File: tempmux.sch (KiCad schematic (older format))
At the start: 15 parts, among them J2 Conn_02x07_Counter_Clockwise, U12 CD74HC4067SM

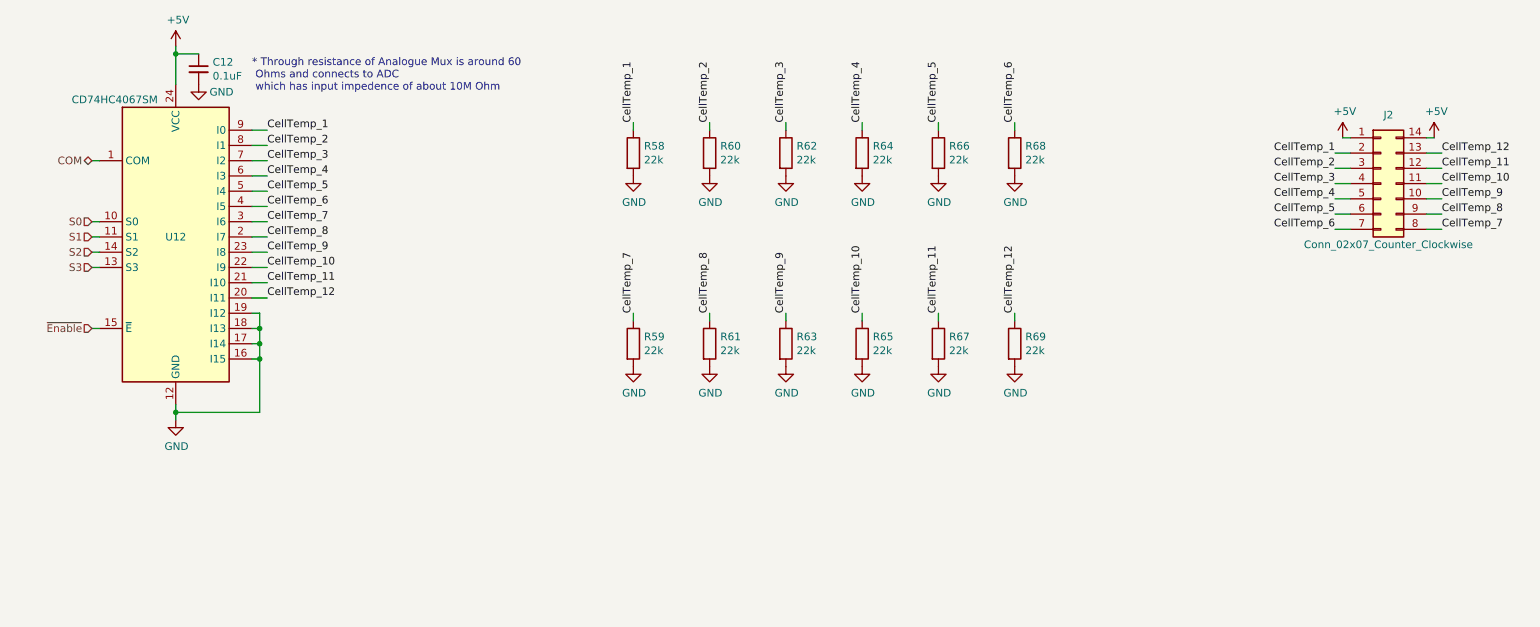
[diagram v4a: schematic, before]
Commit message: Added buttons + redid numbering
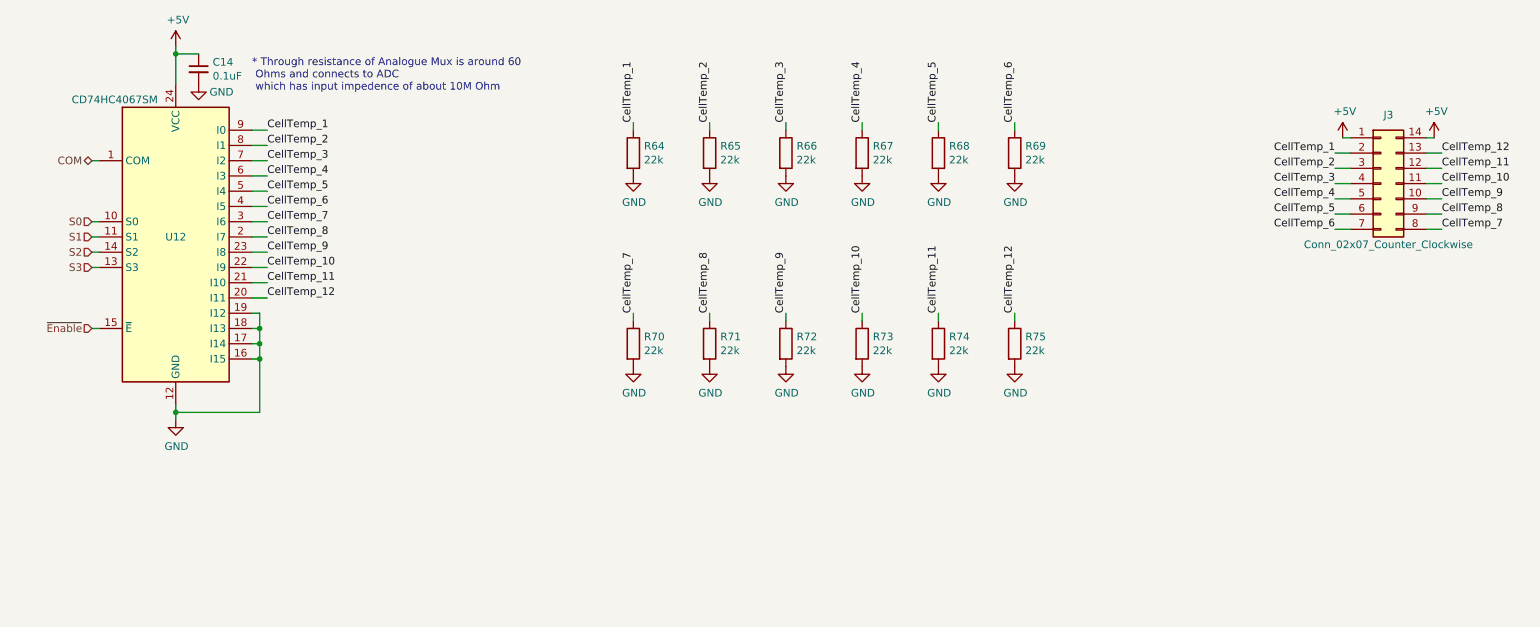
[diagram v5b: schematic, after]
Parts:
- renumbered C12 to C14, J2 to J3, R58 to R64, R60 to R65, R62 to R66, R64 to R67, R66 to R68, R68 to R69, R59 to R70, R61 to R71, R63 to R72, R65 to R73, R67 to R74, R69 to R75
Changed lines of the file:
@@
 P 2000 3400
 AR Path="/5F70A721/5F6868D9" Ref="#PWR?"  Part="1"
-AR Path="/5F70B1A3/5F6868D9" Ref="#PWR0153"  Part="1"
-F 0 "#PWR0153" H 2000 3150 50  0001 C CNN
+AR Path="/5F70B1A3/5F6868D9" Ref="#PWR078"  Part="1"
+F 0 "#PWR078" H 2000 3150 50  0001 C CNN
 F 1 "GND" H 2005 3227 50  0000 C CNN
 F 2 "" H 2000 3400 50  0001 C CNN
@@
 P 2150 1100
 AR Path="/5F70A721/5F6868E0" Ref="C?"  Part="1"
-AR Path="/5F70B1A3/5F6868E0" Ref="C12"  Part="1"
-F 0 "C12" H 2242 1146 50  0000 L CNN
+AR Path="/5F70B1A3/5F6868E0" Ref="C14"  Part="1"
+F 0 "C14" H 2242 1146 50  0000 L CNN
 F 1 "0.1uF" H 2242 1055 50  0000 L CNN
 F 2 "" H 2150 1100 50  0001 C CNN
@@
 P 2150 1200
 AR Path="/5F70A721/5F6868E6" Ref="#PWR?"  Part="1"
-AR Path="/5F70B1A3/5F6868E6" Ref="#PWR0154"  Part="1"
-F 0 "#PWR0154" H 2150 950 50  0001 C CNN
+AR Path="/5F70B1A3/5F6868E6" Ref="#PWR063"  Part="1"
+F 0 "#PWR063" H 2150 950 50  0001 C CNN
 F 1 "GND" H 2300 1150 50  0000 C CNN
 F 2 "" H 2150 1200 50  0001 C CNN
@@
 P 2000 950
 AR Path="/5F70A721/5F6868EC" Ref="#PWR?"  Part="1"
-AR Path="/5F70B1A3/5F6868EC" Ref="#PWR0155"  Part="1"
-F 0 "#PWR0155" H 2000 800 50  0001 C CNN
+AR Path="/5F70B1A3/5F6868EC" Ref="#PWR062"  Part="1"
+F 0 "#PWR062" H 2000 800 50  0001 C CNN
 F 1 "+5V" H 2015 1123 50  0000 C CNN
 F 2 "" H 2000 950 50  0001 C CNN
@@
 P 9900 1850
 AR Path="/5F70A721/5F68B135" Ref="J?"  Part="1"
-AR Path="/5F70B1A3/5F68B135" Ref="J2"  Part="1"
-F 0 "J2" H 9950 2300 50  0000 C CNN
+AR Path="/5F70B1A3/5F68B135" Ref="J3"  Part="1"
+F 0 "J3" H 9950 2300 50  0000 C CNN
 F 1 "Conn_02x07_Counter_Clockwise" H 9950 1450 50  0000 C CNN
 F 2 "" H 9900 1850 50  0001 C CNN
@@
 P 9650 1550
 AR Path="/5F70A721/5F68DF75" Ref="#PWR?"  Part="1"
-AR Path="/5F70B1A3/5F68DF75" Ref="#PWR0156"  Part="1"
-F 0 "#PWR0156" H 9650 1400 50  0001 C CNN
+AR Path="/5F70B1A3/5F68DF75" Ref="#PWR064"  Part="1"
+F 0 "#PWR064" H 9650 1400 50  0001 C CNN
 F 1 "+5V" H 9665 1723 50  0000 C CNN
 F 2 "" H 9650 1550 50  0001 C CNN
@@
 P 10250 1550
 AR Path="/5F70A721/5F68E7C7" Ref="#PWR?"  Part="1"
-AR Path="/5F70B1A3/5F68E7C7" Ref="#PWR0157"  Part="1"
-F 0 "#PWR0157" H 10250 1400 50  0001 C CNN
+AR Path="/5F70B1A3/5F68E7C7" Ref="#PWR065"  Part="1"
+F 0 "#PWR065" H 10250 1400 50  0001 C CNN
 F 1 "+5V" H 10265 1723 50  0000 C CNN
 F 2 "" H 10250 1550 50  0001 C CNN
@@
 	10200 1650 10300 1650
 $Comp
-L Device:R R58
+L Device:R R64
 U 1 1 5F69A862
 P 5000 1650
-F 0 "R58" H 5070 1696 50  0000 L CNN
+F 0 "R64" H 5070 1696 50  0000 L CNN
 F 1 "22k" H 5070 1605 50  0000 L CNN
 F 2 "" V 4930 1650 50  0001 C CNN
@@
 $EndComp
 $Comp
-L Device:R R60
+L Device:R R65
 U 1 1 5F69AE56
 P 5500 1650
-F 0 "R60" H 5570 1696 50  0000 L CNN
+F 0 "R65" H 5570 1696 50  0000 L CNN
 F 1 "22k" H 5570 1605 50  0000 L CNN
 F 2 "" V 5430 1650 50  0001 C CNN
@@
 $EndComp
 $Comp
-L Device:R R62
+L Device:R R66
 U 1 1 5F69AFF2
 P 6000 1650
-F 0 "R62" H 6070 1696 50  0000 L CNN
+F 0 "R66" H 6070 1696 50  0000 L CNN
 F 1 "22k" H 6070 1605 50  0000 L CNN
 F 2 "" V 5930 1650 50  0001 C CNN
@@
 $EndComp
 $Comp
-L Device:R R64
+L Device:R R67
 U 1 1 5F69B1F7
 P 6500 1650
-F 0 "R64" H 6570 1696 50  0000 L CNN
+F 0 "R67" H 6570 1696 50  0000 L CNN
 F 1 "22k" H 6570 1605 50  0000 L CNN
 F 2 "" V 6430 1650 50  0001 C CNN
@@
 $EndComp
 $Comp
-L Device:R R66
+L Device:R R68
 U 1 1 5F69B4CD
 P 7000 1650
-F 0 "R66" H 7070 1696 50  0000 L CNN
+F 0 "R68" H 7070 1696 50  0000 L CNN
 F 1 "22k" H 7070 1605 50  0000 L CNN
 F 2 "" V 6930 1650 50  0001 C CNN
@@
 $EndComp
 $Comp
-L Device:R R68
+L Device:R R69
 U 1 1 5F69B7DC
 P 7500 1650
-F 0 "R68" H 7570 1696 50  0000 L CNN
+F 0 "R69" H 7570 1696 50  0000 L CNN
 F 1 "22k" H 7570 1605 50  0000 L CNN
 F 2 "" V 7430 1650 50  0001 C CNN
@@
 $EndComp
 $Comp
-L Device:R R59
+L Device:R R70
 U 1 1 5F6A3EEE
 P 5000 2900
-F 0 "R59" H 5070 2946 50  0000 L CNN
+F 0 "R70" H 5070 2946 50  0000 L CNN
 F 1 "22k" H 5070 2855 50  0000 L CNN
 F 2 "" V 4930 2900 50  0001 C CNN
@@
 $EndComp
 $Comp
-L Device:R R61
+L Device:R R71
 U 1 1 5F6A3EF4
 P 5500 2900
-F 0 "R61" H 5570 2946 50  0000 L CNN
+F 0 "R71" H 5570 2946 50  0000 L CNN
 F 1 "22k" H 5570 2855 50  0000 L CNN
 F 2 "" V 5430 2900 50  0001 C CNN
@@
 $EndComp
 $Comp
-L Device:R R63
+L Device:R R72
 U 1 1 5F6A3EFA
 P 6000 2900
-F 0 "R63" H 6070 2946 50  0000 L CNN
+F 0 "R72" H 6070 2946 50  0000 L CNN
 F 1 "22k" H 6070 2855 50  0000 L CNN
 F 2 "" V 5930 2900 50  0001 C CNN
@@
 $EndComp
 $Comp
-L Device:R R65
+L Device:R R73
 U 1 1 5F6A3F00
 P 6500 2900
-F 0 "R65" H 6570 2946 50  0000 L CNN
+F 0 "R73" H 6570 2946 50  0000 L CNN
 F 1 "22k" H 6570 2855 50  0000 L CNN
 F 2 "" V 6430 2900 50  0001 C CNN
@@
 $EndComp
 $Comp
-L Device:R R67
+L Device:R R74
 U 1 1 5F6A3F06
 P 7000 2900
-F 0 "R67" H 7070 2946 50  0000 L CNN
+F 0 "R74" H 7070 2946 50  0000 L CNN
 F 1 "22k" H 7070 2855 50  0000 L CNN
 F 2 "" V 6930 2900 50  0001 C CNN
@@
 $EndComp
 $Comp
-L Device:R R69
+L Device:R R75
 U 1 1 5F6A3F0C
 P 7500 2900
-F 0 "R69" H 7570 2946 50  0000 L CNN
+F 0 "R75" H 7570 2946 50  0000 L CNN
 F 1 "22k" H 7570 2855 50  0000 L CNN
 F 2 "" V 7430 2900 50  0001 C CNN
@@
 P 5000 1800
 AR Path="/5F70A721/5F6A4A53" Ref="#PWR?"  Part="1"
-AR Path="/5F70B1A3/5F6A4A53" Ref="#PWR0158"  Part="1"
-F 0 "#PWR0158" H 5000 1550 50  0001 C CNN
+AR Path="/5F70B1A3/5F6A4A53" Ref="#PWR066"  Part="1"
+F 0 "#PWR066" H 5000 1550 50  0001 C CNN
 F 1 "GND" H 5005 1627 50  0000 C CNN
 F 2 "" H 5000 1800 50  0001 C CNN
@@
 P 5500 1800
 AR Path="/5F70A721/5F6A4F23" Ref="#PWR?"  Part="1"
-AR Path="/5F70B1A3/5F6A4F23" Ref="#PWR0159"  Part="1"
-F 0 "#PWR0159" H 5500 1550 50  0001 C CNN
+AR Path="/5F70B1A3/5F6A4F23" Ref="#PWR067"  Part="1"
+F 0 "#PWR067" H 5500 1550 50  0001 C CNN
 F 1 "GND" H 5505 1627 50  0000 C CNN
 F 2 "" H 5500 1800 50  0001 C CNN
@@
 P 6000 1800
 AR Path="/5F70A721/5F6A5197" Ref="#PWR?"  Part="1"
-AR Path="/5F70B1A3/5F6A5197" Ref="#PWR0160"  Part="1"
-F 0 "#PWR0160" H 6000 1550 50  0001 C CNN
+AR Path="/5F70B1A3/5F6A5197" Ref="#PWR068"  Part="1"
+F 0 "#PWR068" H 6000 1550 50  0001 C CNN
 F 1 "GND" H 6005 1627 50  0000 C CNN
 F 2 "" H 6000 1800 50  0001 C CNN
@@
 P 6500 1800
 AR Path="/5F70A721/5F6A5348" Ref="#PWR?"  Part="1"
-AR Path="/5F70B1A3/5F6A5348" Ref="#PWR0161"  Part="1"
-F 0 "#PWR0161" H 6500 1550 50  0001 C CNN
+AR Path="/5F70B1A3/5F6A5348" Ref="#PWR069"  Part="1"
+F 0 "#PWR069" H 6500 1550 50  0001 C CNN
 F 1 "GND" H 6505 1627 50  0000 C CNN
 F 2 "" H 6500 1800 50  0001 C CNN
@@
 P 7000 1800
 AR Path="/5F70A721/5F6A55E5" Ref="#PWR?"  Part="1"
-AR Path="/5F70B1A3/5F6A55E5" Ref="#PWR0162"  Part="1"
-F 0 "#PWR0162" H 7000 1550 50  0001 C CNN
+AR Path="/5F70B1A3/5F6A55E5" Ref="#PWR070"  Part="1"
+F 0 "#PWR070" H 7000 1550 50  0001 C CNN
 F 1 "GND" H 7005 1627 50  0000 C CNN
 F 2 "" H 7000 1800 50  0001 C CNN
@@
 P 7500 1800
 AR Path="/5F70A721/5F6A585F" Ref="#PWR?"  Part="1"
-AR Path="/5F70B1A3/5F6A585F" Ref="#PWR0163"  Part="1"
-F 0 "#PWR0163" H 7500 1550 50  0001 C CNN
+AR Path="/5F70B1A3/5F6A585F" Ref="#PWR071"  Part="1"
+F 0 "#PWR071" H 7500 1550 50  0001 C CNN
 F 1 "GND" H 7505 1627 50  0000 C CNN
 F 2 "" H 7500 1800 50  0001 C CNN
@@
 P 5000 3050
 AR Path="/5F70A721/5F6A59FF" Ref="#PWR?"  Part="1"
-AR Path="/5F70B1A3/5F6A59FF" Ref="#PWR0164"  Part="1"
-F 0 "#PWR0164" H 5000 2800 50  0001 C CNN
+AR Path="/5F70B1A3/5F6A59FF" Ref="#PWR072"  Part="1"
+F 0 "#PWR072" H 5000 2800 50  0001 C CNN
 F 1 "GND" H 5005 2877 50  0000 C CNN
 F 2 "" H 5000 3050 50  0001 C CNN
@@
 P 5500 3050
 AR Path="/5F70A721/5F6A5CE6" Ref="#PWR?"  Part="1"
-AR Path="/5F70B1A3/5F6A5CE6" Ref="#PWR0165"  Part="1"
-F 0 "#PWR0165" H 5500 2800 50  0001 C CNN
+AR Path="/5F70B1A3/5F6A5CE6" Ref="#PWR073"  Part="1"
+F 0 "#PWR073" H 5500 2800 50  0001 C CNN
 F 1 "GND" H 5505 2877 50  0000 C CNN
 F 2 "" H 5500 3050 50  0001 C CNN
@@
 P 6000 3050
 AR Path="/5F70A721/5F6A5EEC" Ref="#PWR?"  Part="1"
-AR Path="/5F70B1A3/5F6A5EEC" Ref="#PWR0166"  Part="1"
-F 0 "#PWR0166" H 6000 2800 50  0001 C CNN
+AR Path="/5F70B1A3/5F6A5EEC" Ref="#PWR074"  Part="1"
+F 0 "#PWR074" H 6000 2800 50  0001 C CNN
 F 1 "GND" H 6005 2877 50  0000 C CNN
 F 2 "" H 6000 3050 50  0001 C CNN
@@
 P 6500 3050
 AR Path="/5F70A721/5F6A6093" Ref="#PWR?"  Part="1"
-AR Path="/5F70B1A3/5F6A6093" Ref="#PWR0167"  Part="1"
-F 0 "#PWR0167" H 6500 2800 50  0001 C CNN
+AR Path="/5F70B1A3/5F6A6093" Ref="#PWR075"  Part="1"
+F 0 "#PWR075" H 6500 2800 50  0001 C CNN
 F 1 "GND" H 6505 2877 50  0000 C CNN
 F 2 "" H 6500 3050 50  0001 C CNN
@@
 P 7000 3050
 AR Path="/5F70A721/5F6A622C" Ref="#PWR?"  Part="1"
-AR Path="/5F70B1A3/5F6A622C" Ref="#PWR0168"  Part="1"
-F 0 "#PWR0168" H 7000 2800 50  0001 C CNN
+AR Path="/5F70B1A3/5F6A622C" Ref="#PWR076"  Part="1"
+F 0 "#PWR076" H 7000 2800 50  0001 C CNN
 F 1 "GND" H 7005 2877 50  0000 C CNN
 F 2 "" H 7000 3050 50  0001 C CNN
@@
 P 7500 3050
 AR Path="/5F70A721/5F6A6421" Ref="#PWR?"  Part="1"
-AR Path="/5F70B1A3/5F6A6421" Ref="#PWR0169"  Part="1"
-F 0 "#PWR0169" H 7500 2800 50  0001 C CNN
+AR Path="/5F70B1A3/5F6A6421" Ref="#PWR077"  Part="1"
+F 0 "#PWR077" H 7500 2800 50  0001 C CNN
 F 1 "GND" H 7505 2877 50  0000 C CNN
 F 2 "" H 7500 3050 50  0001 C CNN

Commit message: Added PCB temp sensors and redit numberings
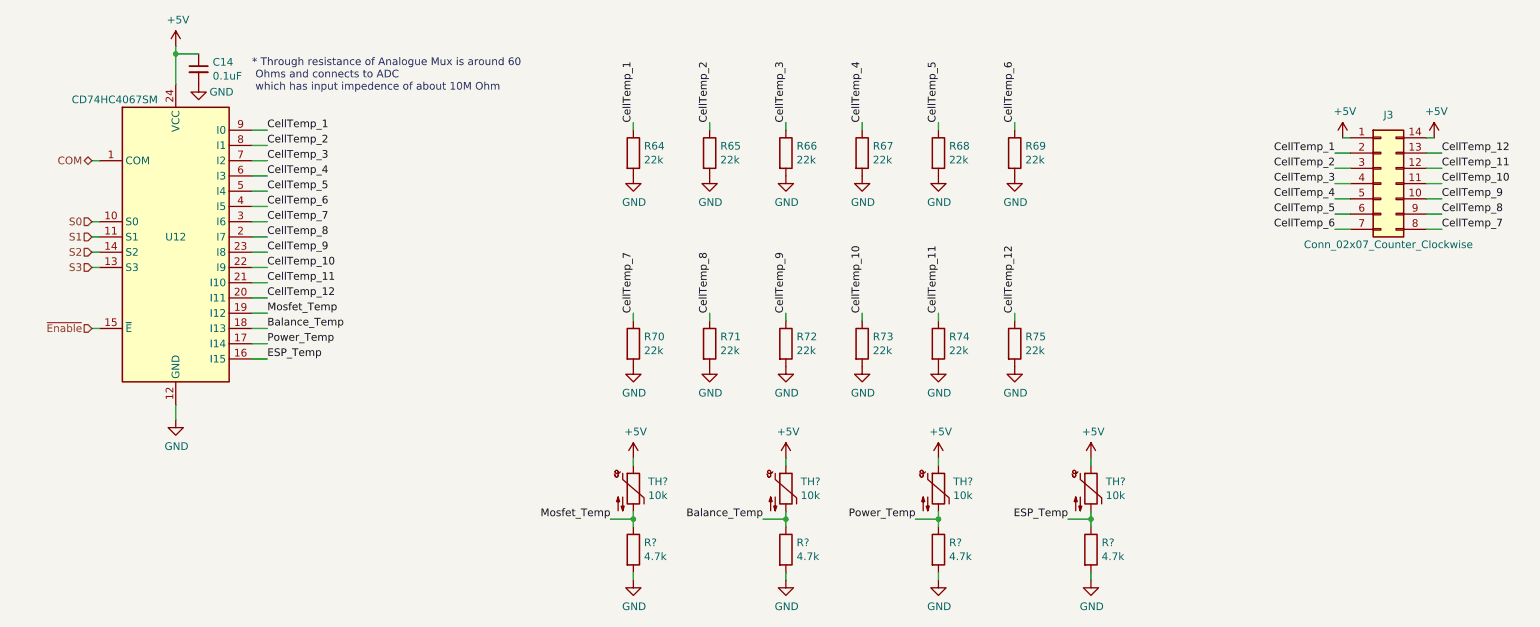
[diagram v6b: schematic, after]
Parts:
- added R? (x4): 4.7k, symbol Device:R
- added TH? (x4): 10k, symbol Device:Thermistor_NTC
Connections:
- net +5V: now also TH?.1, TH?.1, TH?.1, TH?.1
- net GND: now also R?.2, R?.2, R?.2, R?.2; no longer U12.16 (I15), U12.17 (I14), U12.18 (I13), U12.19 (I12)
- new net Balance_Temp: R?.1, TH?.2, U12.18 (I13)
- new net ESP_Temp: R?.1, TH?.2, U12.16 (I15)
- new net Mosfet_Temp: R?.1, TH?.2, U12.19 (I12)
- new net Power_Temp: R?.1, TH?.2, U12.17 (I14)
